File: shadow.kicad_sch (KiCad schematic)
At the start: 12 parts, among them SW1 SW_Push, SW2 SW_Push

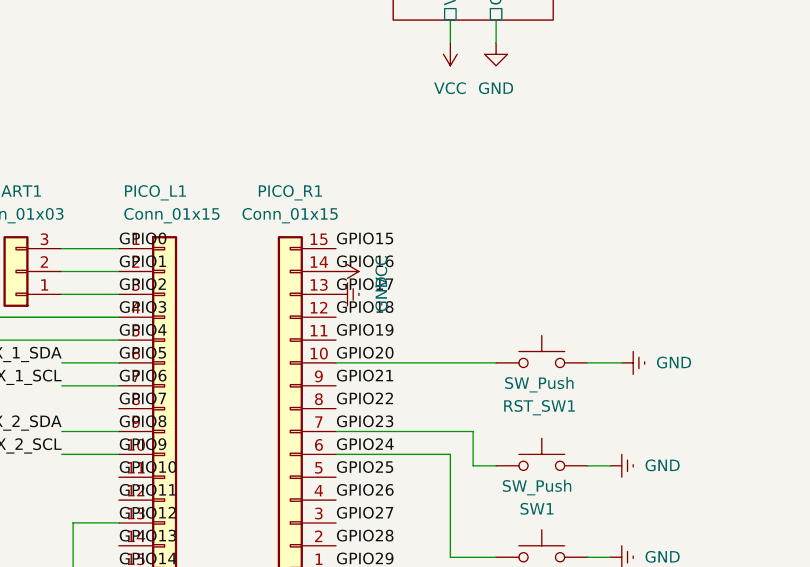
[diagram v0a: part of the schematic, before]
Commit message: Add new lipo charger to pcb
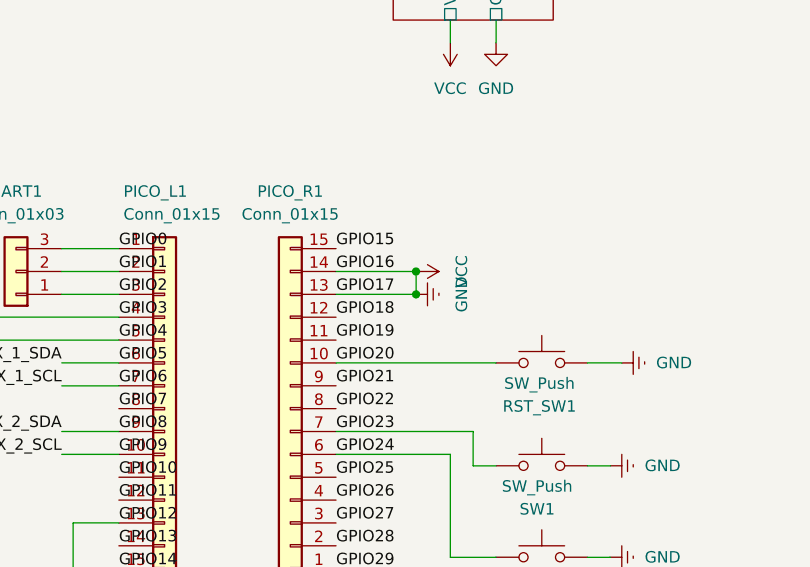
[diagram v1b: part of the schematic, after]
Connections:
- net VCC is gone; now on net GND: GPIO_R1.14 (Pin_14), OLED_CONN1.1 (Pin_1), PICO_R1.14 (Pin_14), SENSOR_CONN1.3 (Pin_3), US_SENSOR_CONN1.3 (Pin_3)

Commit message: a lot of work on pcb
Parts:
- added BATT_JST1: JST, Connector_JST:JST_XH_B2B-XH-A_1x02_P2.50mm_Vertical, symbol Connector_Generic:Conn_01x02
- renumbered SENSOR_CONN1 to ARR1, US_SENSOR_CONN1 to US1
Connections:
- net GND: no longer ARR1.3 (Pin_3), GPIO_R1.14 (Pin_14), OLED_CONN1.1 (Pin_1), PICO_R1.14 (Pin_14), US1.3 (Pin_3)
- new net VCC: ARR1.3 (Pin_3), GPIO_R1.14 (Pin_14), OLED_CONN1.1 (Pin_1), PICO_R1.14 (Pin_14), US1.3 (Pin_3)
- new net battery/BAT+: BATT_JST1.1 (Pin_1)
- new net battery/BAT-: BATT_JST1.2 (Pin_2)
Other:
- sheet battery ports: added BAT+, BAT-; removed none
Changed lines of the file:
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@@
 		(comment 1 "Shenanigans are afoot :)")
 	)
-	(junction
-		(at 142.24 96.52)
-		(diameter 0)
-		(color 0 0 0 0)
-	)
-	(junction
-		(at 142.24 93.98)
-		(diameter 0)
-		(color 0 0 0 0)
-	)
 	(wire
 		(pts
@@
 	(wire
 		(pts
-			(xy 142.24 93.98) (xy 142.24 96.52)
-		)
-		(stroke
-			(width 0)
-			(type default)
-		)
-	)
-	(wire
-		(pts
 			(xy 229.87 68.58) (xy 229.87 66.04)
 		)
@@
 	)
 	(symbol
+		(lib_id "Connector_Generic:Conn_01x02")
+		(at 66.04 31.75 180)
+		(unit 1)
+		(exclude_from_sim no)
+		(in_bom yes)
+		(on_board yes)
+		(dnp no)
+		(fields_autoplaced yes)
+		(property "Reference" "BATT_JST1"
+			(at 66.04 22.86 0)
+			(effects
+				(font
+					(size 1.27 1.27)
+				)
+			)
+		)
+		(property "Value" "JST"
+			(at 66.04 25.4 0)
+			(effects
+				(font
+					(size 1.27 1.27)
+				)
+			)
+		)
+		(property "Footprint" "Connector_JST:JST_XH_B2B-XH-A_1x02_P2.50mm_Vertical"
+			(at 66.04 31.75 0)
+			(effects
+				(font
+					(size 1.27 1.27)
+				)
+				(hide yes)
+			)
+		)
+		(property "Datasheet" "~"
+			(at 66.04 31.75 0)
+			(effects
+				(font
+					(size 1.27 1.27)
+				)
+				(hide yes)
+			)
+		)
+		(property "Description" "Generic connector, single row, 01x02, script generated (kicad-library-utils/schlib/autogen/connector/)"
+			(at 66.04 31.75 0)
+			(effects
+				(font
+					(size 1.27 1.27)
+				)
+				(hide yes)
+			)
+		)
+		(pin "1"
+		)
+		(pin "2"
+		)
+		(instances
+			(project ""
+				(path "/3c2fce68-ba60-4bda-a294-ddd60ff77106"
+					(reference "BATT_JST1")
+					(unit 1)
+				)
+			)
+		)
+	)
+	(symbol
 		(lib_id "power:VCC")
 		(at 78.74 53.34 180)
@@
 		(dnp no)
 		(fields_autoplaced yes)
-		(property "Reference" "SENSOR_CONN1"
+		(property "Reference" "ARR1"
 			(at 238.76 99.0599 0)
 			(effects
@@
 			(project "shadow"
 				(path "/3c2fce68-ba60-4bda-a294-ddd60ff77106"
-					(reference "SENSOR_CONN1")
+					(reference "ARR1")
 					(unit 1)
 				)
@@
 		(dnp no)
 		(fields_autoplaced yes)
-		(property "Reference" "US_SENSOR_CONN1"
+		(property "Reference" "US1"
 			(at 238.76 113.0299 0)
 			(effects
@@
 			(project "shadow"
 				(path "/3c2fce68-ba60-4bda-a294-ddd60ff77106"
-					(reference "US_SENSOR_CONN1")
+					(reference "US1")
 					(unit 1)
 				)
@@
 			(effects
 				(font
+					(size 1.27 1.27)
+				)
+				(justify left)
+			)
+		)
+		(pin "BAT+" passive
+			(at 71.12 31.75 180)
+			(effects
+				(font
+					(size 1.27 1.27)
+				)
+				(justify left)
+			)
+		)
+		(pin "BAT-" passive
+			(at 71.12 29.21 180)
+			(effects
+				(font

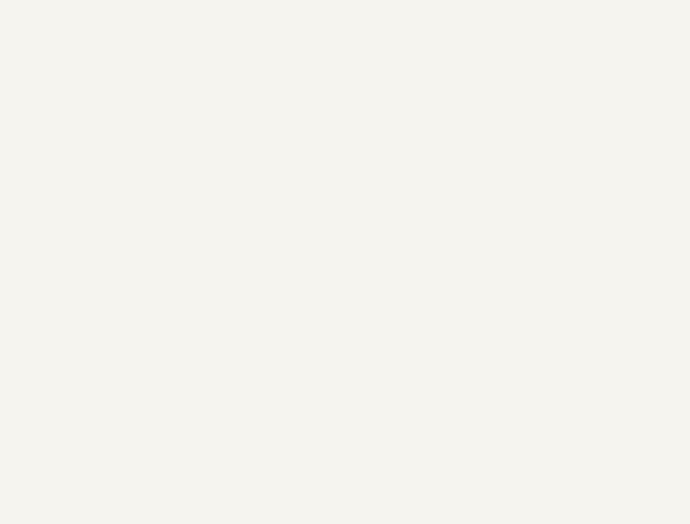
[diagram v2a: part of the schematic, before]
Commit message: ground mounting holes
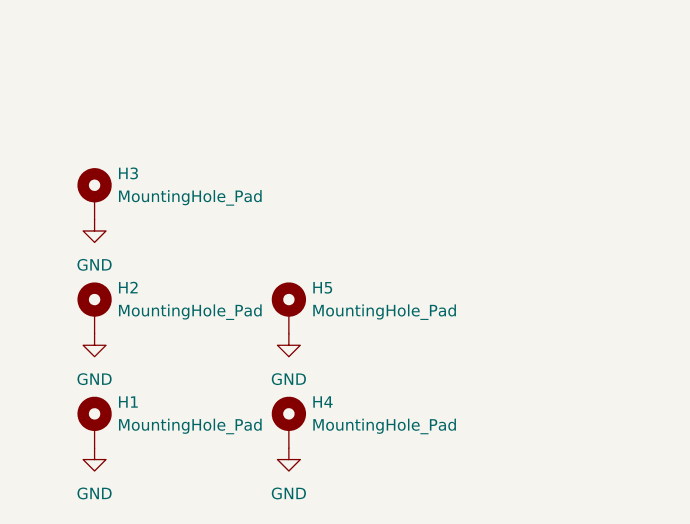
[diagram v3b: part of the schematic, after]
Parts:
- added H1, H2, H3, H4, H5: MountingHole_Pad, MountingHole:MountingHole_4.3mm_M4_DIN965_Pad, symbol Mechanical:MountingHole_Pad
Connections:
- net GND: now also H1.1, H2.1, H3.1, H4.1, H5.1

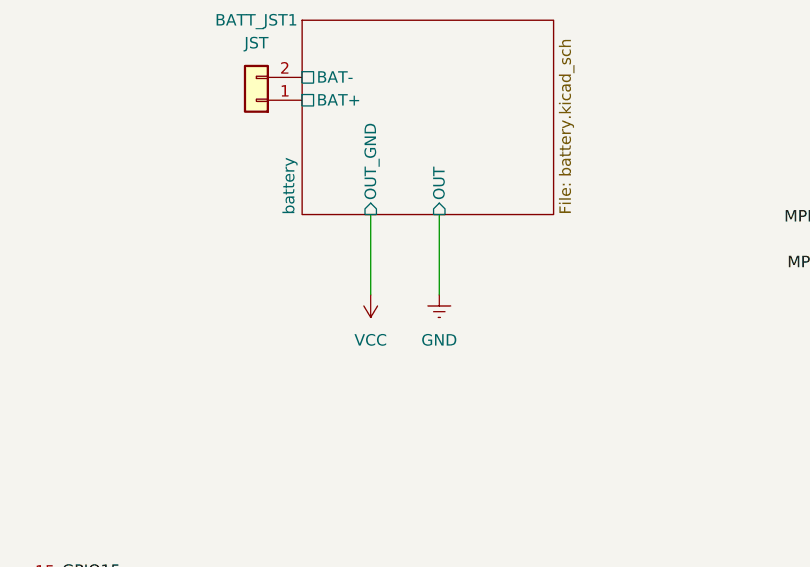
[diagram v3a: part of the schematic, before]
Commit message: Update to new cap footprint
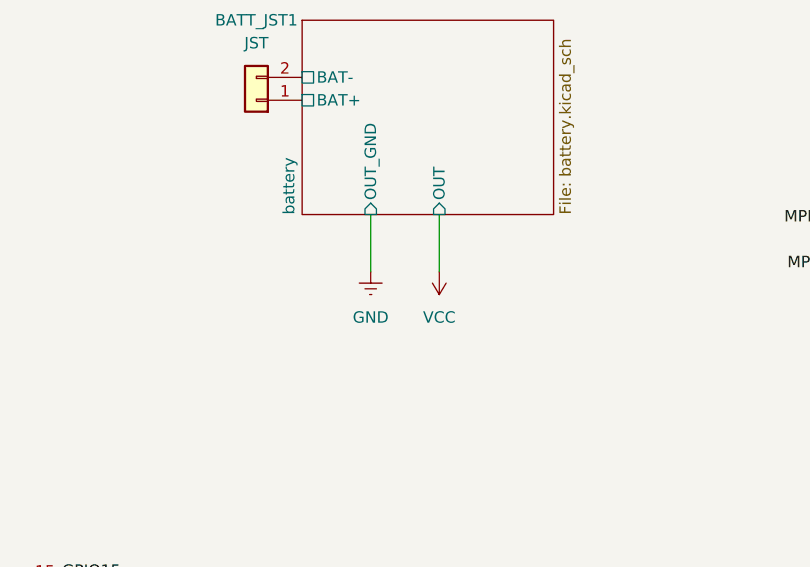
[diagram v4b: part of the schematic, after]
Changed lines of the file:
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@@
 	(wire
 		(pts
-			(xy 78.74 44.45) (xy 78.74 53.34)
+			(xy 78.74 44.45) (xy 78.74 50.8)
 		)
 		(stroke
@@
 	(wire
 		(pts
+			(xy 86.36 50.8) (xy 86.36 44.45)
+		)
+		(stroke
+			(width 0)
+			(type default)
+		)
+	)
+	(wire
+		(pts
 			(xy 163.83 125.73) (xy 161.29 125.73)
 		)
@@
 	(wire
 		(pts
-			(xy 86.36 44.45) (xy 86.36 53.34)
-		)
-		(stroke
-			(width 0)
-			(type default)
-		)
-	)
-	(wire
-		(pts
 			(xy 102.87 114.3) (xy 109.22 114.3)
 		)
@@
 	(symbol
 		(lib_id "power:VCC")
-		(at 78.74 53.34 180)
+		(at 86.36 50.8 180)
 		(unit 1)
 		(exclude_from_sim no)
@@
 		(fields_autoplaced yes)
 		(property "Reference" "#PWR01"
-			(at 78.74 49.53 0)
+			(at 86.36 46.99 0)
 			(effects
 				(font
@@
 		)
 		(property "Value" "VCC"
-			(at 78.74 58.42 0)
+			(at 86.36 55.88 0)
 			(effects
 				(font
@@
 		)
 		(property "Footprint" ""
-			(at 78.74 53.34 0)
+			(at 86.36 50.8 0)
 			(effects
 				(font
@@
 		)
 		(property "Datasheet" ""
-			(at 78.74 53.34 0)
+			(at 86.36 50.8 0)
 			(effects
 				(font
@@
 		)
 		(property "Description" "Power symbol creates a global label with name \"VCC\""
-			(at 78.74 53.34 0)
+			(at 86.36 50.8 0)
 			(effects
 				(font
@@
 	(symbol
 		(lib_id "power:Earth")
-		(at 86.36 53.34 0)
+		(at 78.74 50.8 0)
 		(unit 1)
 		(exclude_from_sim no)
@@
 		(fields_autoplaced yes)
 		(property "Reference" "#PWR03"
-			(at 86.36 59.69 0)
+			(at 78.74 57.15 0)
 			(effects
 				(font
@@
 		)
 		(property "Value" "GND"
-			(at 86.36 58.42 0)
+			(at 78.74 55.88 0)
 			(effects
 				(font
@@
 		)
 		(property "Footprint" ""
-			(at 86.36 53.34 0)
+			(at 78.74 50.8 0)
 			(effects
 				(font
@@
 		)
 		(property "Datasheet" "~"
-			(at 86.36 53.34 0)
+			(at 78.74 50.8 0)
 			(effects
 				(font
@@
 		)
 		(property "Description" "Power symbol creates a global label with name \"Earth\""
-			(at 86.36 53.34 0)
+			(at 78.74 50.8 0)
 			(effects
 				(font

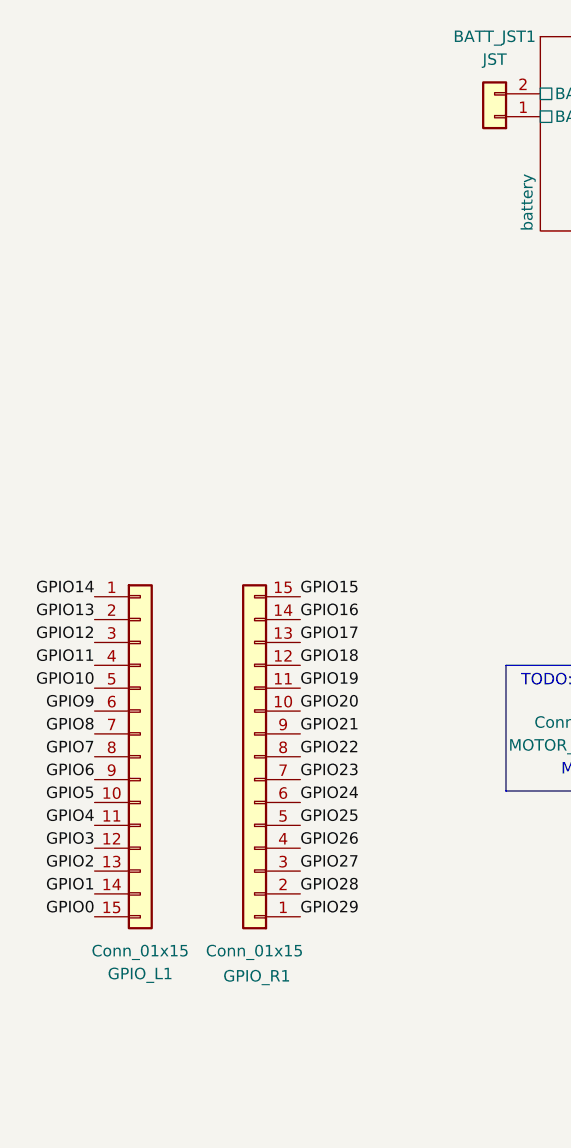
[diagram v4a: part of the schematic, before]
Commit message: fix pico mount width and orientation of left gpio
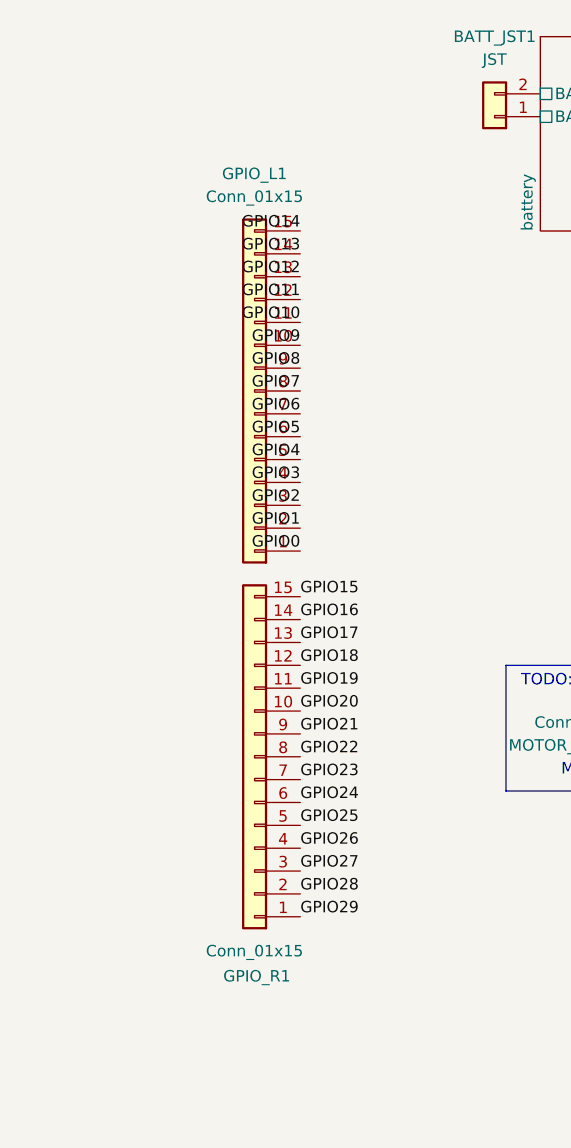
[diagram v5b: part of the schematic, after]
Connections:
- net GND: now also GPIO_L1.13 (Pin_13); no longer GPIO_L1.3 (Pin_3)
- net GPIO0: now also GPIO_L1.1 (Pin_1); no longer GPIO_L1.15 (Pin_15)
- net GPIO1: now also GPIO_L1.2 (Pin_2); no longer GPIO_L1.14 (Pin_14)
- net GPIO10: now also GPIO_L1.11 (Pin_11); no longer GPIO_L1.5 (Pin_5)
- net GPIO11: now also GPIO_L1.12 (Pin_12); no longer GPIO_L1.4 (Pin_4)
- net GPIO13: now also GPIO_L1.14 (Pin_14); no longer GPIO_L1.2 (Pin_2)
- net GPIO14: now also GPIO_L1.15 (Pin_15); no longer GPIO_L1.1 (Pin_1)
- net GPIO2: now also GPIO_L1.3 (Pin_3); no longer GPIO_L1.13 (Pin_13)
- net GPIO3: now also GPIO_L1.4 (Pin_4); no longer GPIO_L1.12 (Pin_12)
- net GPIO4: now also GPIO_L1.5 (Pin_5); no longer GPIO_L1.11 (Pin_11)
- net GPIO5: now also GPIO_L1.6 (Pin_6); no longer GPIO_L1.10 (Pin_10)
- net GPIO6: now also GPIO_L1.7 (Pin_7); no longer GPIO_L1.9 (Pin_9)
- net GPIO8: now also GPIO_L1.9 (Pin_9); no longer GPIO_L1.7 (Pin_7)
- net GPIO9: now also GPIO_L1.10 (Pin_10); no longer GPIO_L1.6 (Pin_6)
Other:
- moved on the sheet: GPIO_L1
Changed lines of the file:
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@@
-		)
-	)
-	(label "GPIO14"
-		(at 21.59 85.09 180)
-		(fields_autoplaced yes)
-		(effects
-			(font
-				(size 1.27 1.27)
-			)
-			(justify right bottom)
 		)
 	)
@@
 		)
 	)
+	(label "GPIO13"
+		(at 44.45 46.99 180)
+		(fields_autoplaced yes)
+		(effects
+			(font
+				(size 1.27 1.27)
+			)
+			(justify right bottom)
+		)
+	)
 	(label "GPIO25"
 		(at 44.45 110.49 0)
@@
 		)
 	)
+	(label "GPIO1"
+		(at 44.45 77.47 180)
+		(fields_autoplaced yes)
+		(effects
+			(font
+				(size 1.27 1.27)
+			)
+			(justify right bottom)
+		)
+	)
 	(label "GPIO20"
 		(at 133.35 104.14 0)
@@
 		)
 	)
-	(label "GPIO8"
-		(at 21.59 100.33 180)
+	(label "GPIO0"
+		(at 44.45 80.01 180)
 		(fields_autoplaced yes)
 		(effects
@@
 		)
 	)
-	(label "GPIO10"
-		(at 21.59 95.25 180)
-		(fields_autoplaced yes)
-		(effects
-			(font
-				(size 1.27 1.27)
-			)
-			(justify right bottom)
-		)
-	)
 	(label "MPLX_1_SDA"
 		(at 102.87 104.14 180)
@@
 		)
 	)
+	(label "GPIO14"
+		(at 44.45 44.45 180)
+		(fields_autoplaced yes)
+		(effects
+			(font
+				(size 1.27 1.27)
+			)
+			(justify right bottom)
+		)
+	)
 	(label "GPIO18"
 		(at 44.45 92.71 0)
@@
 		)
 	)
+	(label "GPIO12"
+		(at 44.45 49.53 180)
+		(fields_autoplaced yes)
+		(effects
+			(font
+				(size 1.27 1.27)
+			)
+			(justify right bottom)
+		)
+	)
 	(label "GPIO0"
 		(at 109.22 91.44 0)
@@
 		)
 	)
+	(label "GPIO2"
+		(at 44.45 74.93 180)
+		(fields_autoplaced yes)
+		(effects
+			(font
+				(size 1.27 1.27)
+			)
+			(justify right bottom)
+		)
+	)
 	(label "GPIO4"
 		(at 109.22 101.6 0)
@@
 		)
 	)
-	(label "GPIO4"
-		(at 21.59 110.49 180)
+	(label "GPIO8"
+		(at 44.45 59.69 180)
 		(fields_autoplaced yes)
 		(effects
@@
 		)
 	)
-	(label "GPIO6"
-		(at 21.59 105.41 180)
-		(fields_autoplaced yes)
-		(effects
-			(font
-				(size 1.27 1.27)
-			)
-			(justify right bottom)
-		)
-	)
-	(label "GPIO2"
-		(at 21.59 115.57 180)
-		(fields_autoplaced yes)
-		(effects
-			(font
-				(size 1.27 1.27)
-			)
-			(justify right bottom)
-		)
-	)
-	(label "GPIO5"
-		(at 21.59 107.95 180)
-		(fields_autoplaced yes)
-		(effects
-			(font
-				(size 1.27 1.27)
-			)
-			(justify right bottom)
-		)
-	)
 	(label "MPLX_2_SCL"
 		(at 219.71 50.8 180)
@@
 		)
 	)
-	(label "GPIO12"
-		(at 21.59 90.17 180)
-		(fields_autoplaced yes)
-		(effects
-			(font
-				(size 1.27 1.27)
-			)
-			(justify right bottom)
-		)
-	)
-	(label "GPIO1"
-		(at 21.59 118.11 180)
+	(label "GPIO3"
+		(at 44.45 72.39 180)
+		(fields_autoplaced yes)
+		(effects
+			(font
+				(size 1.27 1.27)
+			)
+			(justify right bottom)
+		)
+	)
+	(label "GPIO4"
+		(at 44.45 69.85 180)
 		(fields_autoplaced yes)
 		(effects
@@
 		)
 	)
+	(label "GPIO11"
+		(at 44.45 52.07 180)
+		(fields_autoplaced yes)
+		(effects
+			(font
+				(size 1.27 1.27)
+			)
+			(justify right bottom)
+		)
+	)
 	(label "GPIO28"
 		(at 133.35 124.46 0)
@@
 		)
 	)
-	(label "GPIO0"
-		(at 21.59 120.65 180)
-		(fields_autoplaced yes)
-		(effects
-			(font
-				(size 1.27 1.27)
-			)
-			(justify right bottom)
-		)
-	)
 	(label "GPIO17"
 		(at 133.35 96.52 0)
@@
 		)
 	)
-	(label "GPIO3"
-		(at 21.59 113.03 180)
+	(label "GPIO5"
+		(at 44.45 67.31 180)
 		(fields_autoplaced yes)
 		(effects
@@
 		)
 	)
+	(label "GPIO6"
+		(at 44.45 64.77 180)
+		(fields_autoplaced yes)
+		(effects
+			(font
+				(size 1.27 1.27)
+			)
+			(justify right bottom)
+		)
+	)
 	(label "OLED_SDA"
 		(at 219.71 90.17 180)
@@
 		)
 	)
+	(label "GPIO9"
+		(at 44.45 57.15 180)
+		(fields_autoplaced yes)
+		(effects
+			(font
+				(size 1.27 1.27)
+			)
+			(justify right bottom)
+		)
+	)
+	(label "GPIO10"
+		(at 44.45 54.61 180)
+		(fields_autoplaced yes)
+		(effects
+			(font
+				(size 1.27 1.27)
+			)
+			(justify right bottom)
+		)
+	)
 	(label "GPIO11"
 		(at 109.22 119.38 0)
@@
 		)
 	)
-	(label "GPIO13"
-		(at 21.59 87.63 180)
-		(fields_autoplaced yes)
-		(effects
-			(font
-				(size 1.27 1.27)
-			)
-			(justify right bottom)
-		)
-	)
-	(label "GPIO9"
-		(at 21.59 97.79 180)
-		(fields_autoplaced yes)
-		(effects
-			(font
-				(size 1.27 1.27)
-			)
-			(justify right bottom)
-		)
-	)
 	(label "GPIO7"
 		(at 109.22 109.22 0)
@@
 		)
 	)
+	(label "GPIO7"
+		(at 44.45 62.23 180)
+		(fields_autoplaced yes)
+		(effects
+			(font
+				(size 1.27 1.27)
+			)
+			(justify right bottom)
+		)
+	)
 	(label "OLED_SCL"
 		(at 219.71 87.63 180)
@@
 		)
 	)
-	(label "GPIO11"
-		(at 21.59 92.71 180)
-		(fields_autoplaced yes)
-		(effects
-			(font
-				(size 1.27 1.27)
-			)
-			(justify right bottom)
-		)
-	)
 	(label "US_SCL"
 		(at 226.06 113.03 180)
@@
 			)
 			(justify left bottom)
-		)
-	)
-	(label "GPIO7"
-		(at 21.59 102.87 180)
-		(fields_autoplaced yes)
-		(effects
-			(font
-				(size 1.27 1.27)
-			)
-			(justify right bottom)
 		)
 	)
@@
 	(symbol
 		(lib_id "Connector_Generic:Conn_01x15")
-		(at 26.67 102.87 0)
+		(at 39.37 62.23 180)
 		(unit 1)
 		(exclude_from_sim no)
@@
 		(fields_autoplaced yes)
 		(property "Reference" "GPIO_L1"
-			(at 26.67 127 0)
+			(at 39.37 38.1 0)
 			(effects
 				(font
@@
 		)
 		(property "Value" "Conn_01x15"
-			(at 26.67 124.46 0)
+			(at 39.37 40.64 0)
 			(effects
 				(font
@@
 		)
 		(property "Footprint" "Connector_PinSocket_2.54mm:PinSocket_1x15_P2.54mm_Vertical"
-			(at 26.67 102.87 0)
+			(at 39.37 62.23 0)
 			(effects
 				(font
@@
 		)
 		(property "Datasheet" "~"
-			(at 26.67 102.87 0)
+			(at 39.37 62.23 0)
 			(effects
 				(font
@@
 		)
 		(property "Description" "Generic connector, single row, 01x15, script generated (kicad-library-utils/schlib/autogen/connector/)"
-			(at 26.67 102.87 0)
-			(effects
-				(font
+			(at 39.37 62.23 0)
+			(effects
+				(font

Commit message: fix some stuff and retrace
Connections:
- net GND: now also GPIO_R1.3 (Pin_3), PICO_R1.3 (Pin_3); no longer GPIO_R1.13 (Pin_13), PICO_R1.13 (Pin_13)
- net GPIO15: now also GPIO_R1.1 (Pin_1), PICO_R1.1 (Pin_1); no longer GPIO_R1.15 (Pin_15), PICO_R1.15 (Pin_15)
- net GPIO18: now also GPIO_R1.4 (Pin_4), PICO_R1.4 (Pin_4); no longer GPIO_R1.12 (Pin_12), PICO_R1.12 (Pin_12)
- net GPIO19: now also GPIO_R1.5 (Pin_5), PICO_R1.5 (Pin_5); no longer GPIO_R1.11 (Pin_11), PICO_R1.11 (Pin_11)
- net GPIO20: now also GPIO_R1.6 (Pin_6), PICO_R1.6 (Pin_6); no longer GPIO_R1.10 (Pin_10), PICO_R1.10 (Pin_10)
- net GPIO21: now also GPIO_R1.7 (Pin_7), PICO_R1.7 (Pin_7); no longer GPIO_R1.9 (Pin_9), PICO_R1.9 (Pin_9)
- net GPIO23: now also GPIO_R1.9 (Pin_9), PICO_R1.9 (Pin_9); no longer GPIO_R1.7 (Pin_7), PICO_R1.7 (Pin_7)
- net GPIO24: now also GPIO_R1.10 (Pin_10), PICO_R1.10 (Pin_10); no longer GPIO_R1.6 (Pin_6), PICO_R1.6 (Pin_6)
- net GPIO25: now also GPIO_R1.11 (Pin_11), PICO_R1.11 (Pin_11); no longer GPIO_R1.5 (Pin_5), PICO_R1.5 (Pin_5)
- net GPIO26: now also GPIO_R1.12 (Pin_12), PICO_R1.12 (Pin_12); no longer GPIO_R1.4 (Pin_4), PICO_R1.4 (Pin_4)
- net GPIO27: now also GPIO_R1.13 (Pin_13), PICO_R1.13 (Pin_13); no longer GPIO_R1.3 (Pin_3), PICO_R1.3 (Pin_3)
- net GPIO28: now also GPIO_R1.14 (Pin_14), PICO_R1.14 (Pin_14); no longer GPIO_R1.2 (Pin_2), PICO_R1.2 (Pin_2)
- net GPIO29: now also GPIO_R1.15 (Pin_15), PICO_R1.15 (Pin_15); no longer GPIO_R1.1 (Pin_1), PICO_R1.1 (Pin_1)
- net VCC: now also GPIO_R1.2 (Pin_2), PICO_R1.2 (Pin_2); no longer GPIO_R1.14 (Pin_14), PICO_R1.14 (Pin_14)
